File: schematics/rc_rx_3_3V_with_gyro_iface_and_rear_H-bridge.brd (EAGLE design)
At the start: 63.5 x 45.7 mm, 45 parts, among them IC1 PIC16F1826/27SO, IC2 LD117AS50TR, Q1 IRF3704S, Q2 IRF3704S, Q3 IRF7309, Q4 IRF7309, Q5 BSS123, Q6 BSS123

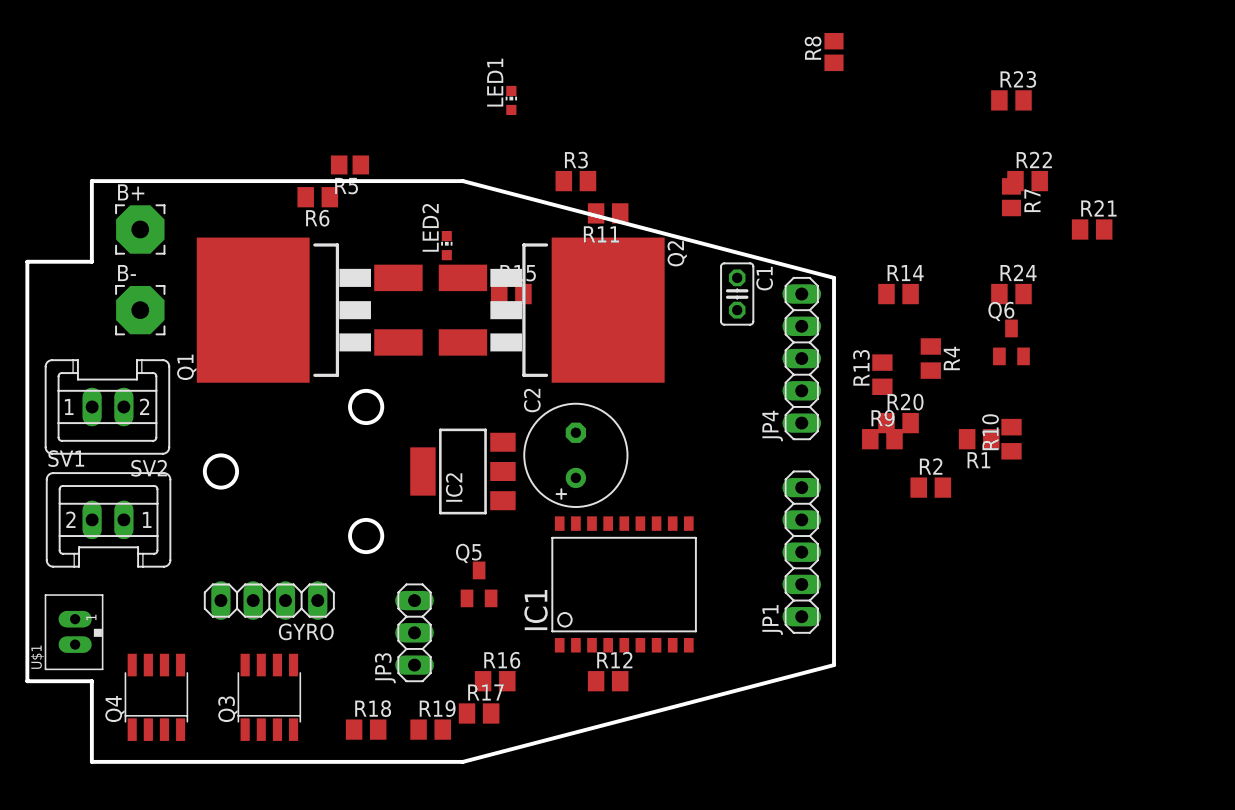
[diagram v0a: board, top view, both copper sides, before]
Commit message: Working on broken ADC and MSSP
This commit is to show to Microchip
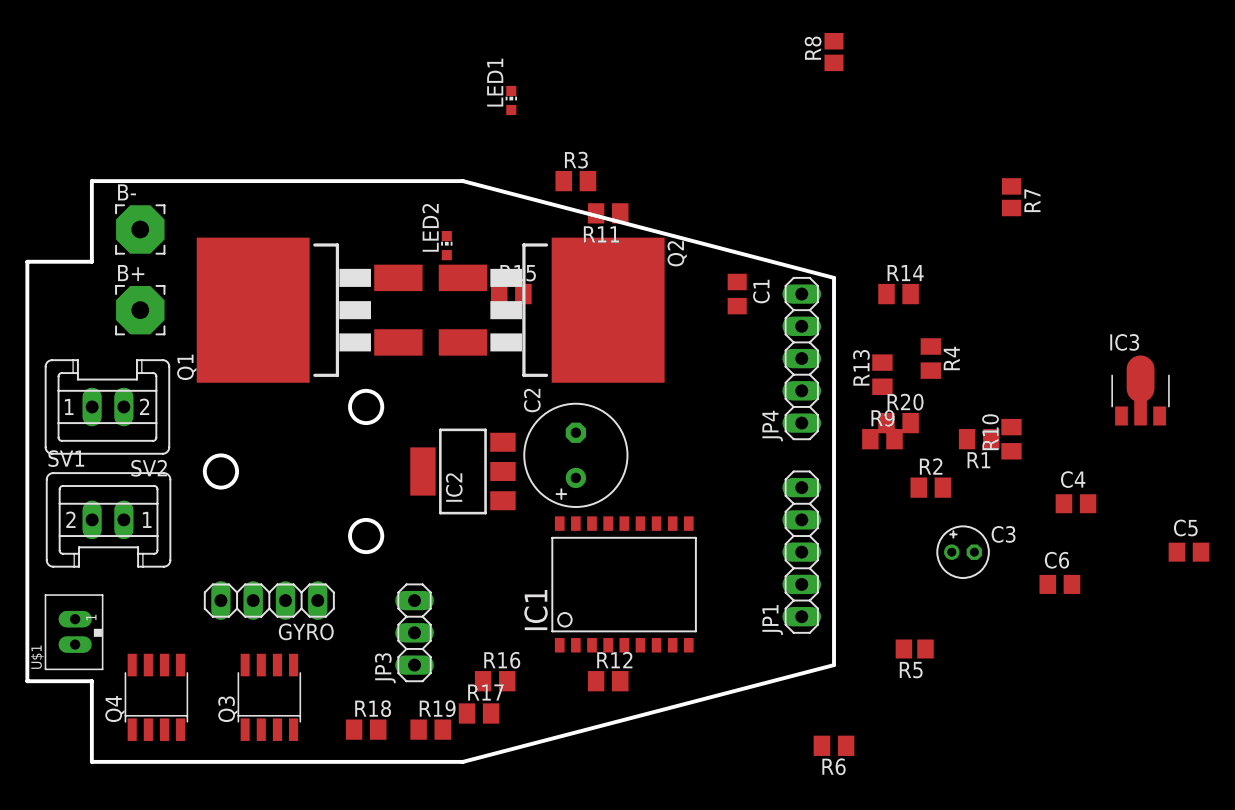
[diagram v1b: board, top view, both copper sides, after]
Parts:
- removed Q5, Q6: BSS123, transistor-small-signal:SOT23
- removed R21, R22, R23, R24: 4k7, resistor:M0805
- added C3: 4.7uF, rcl:E1,8-4
- added C4: 100nF, rcl:C0805
- added C5, C6: 0.1uF, rcl:C0805
- added IC3: 78L05F, linear:SOT89
- C1: device rcl:C025-025X050 -> rcl:C0805
- R14, R15: value 1k -> 470
- moved R6 59.3 mm to (63.5, 1.27)
- moved R5 58.5 mm to (69.8, 8.89)
- moved B+ 6.35 mm to (8.89, 35.6)
- moved B- 6.35 mm to (8.89, 41.9)
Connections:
- new net +12V: C6.1, IC3.3
- net 3.3V: now also C3.+, C5.1, IC3.1; no longer Q5.1, Q6.1, R21.1, R22.1
- net 5V: now also C4.1; no longer C2.+
- net GND: now also C3.-, C4.2, C5.2, C6.2, IC3.2, IC3.2@1
- net SCL_3.3: no longer Q6.2, R22.2
- net SCL_5: no longer Q6.3, R24.2
- net SDA_3.3: no longer Q5.2, R21.2
- net SDA_5: no longer Q5.3, R23.2
- net V+: now also C2.+
- net VDD: no longer R23.1, R24.1
